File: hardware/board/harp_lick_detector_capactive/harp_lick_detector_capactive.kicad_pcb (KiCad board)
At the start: 4 copper layers, 80 x 50 mm, 132 parts, among them J1 Conn_Coaxial, J2 Conn_01x03_Male, J3 Conn_Triaxial, J4 AudioJack3, J5 USB_C_Receptacle_USB2.0, J6 Barrel_Jack_Switch, J7 Conn_Coaxial, SW1 SW_Push, U10 CD74AC04, U11 LM27762, U12 LT3030, U13 ADS7049, U2 TPD2EUSB30, U3 ADUM4160, U4 RP2040, U5 W25Q128JVS, U6 LTC6263, U7 LTC6268xS8-10, U8 REF3433QDBVRQ1, U9 AD9833xRM, X1 ECS-TXO-2016

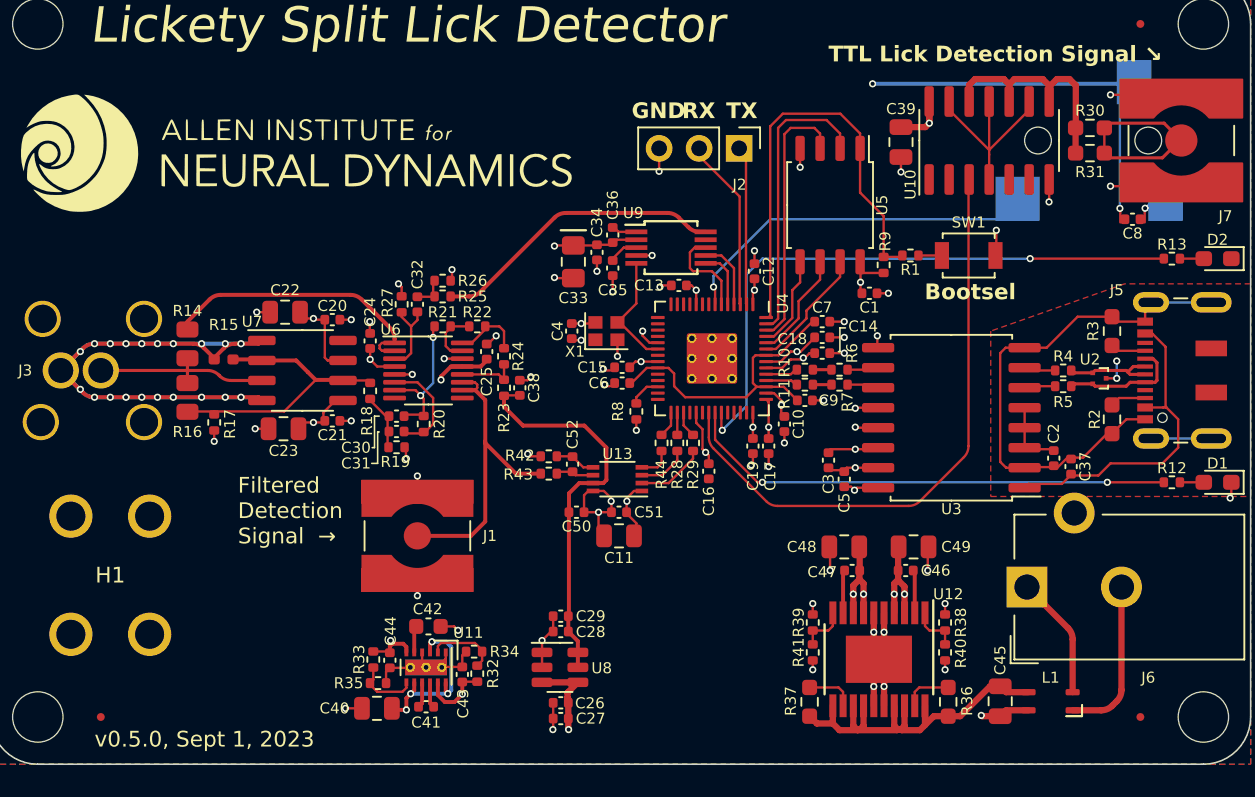
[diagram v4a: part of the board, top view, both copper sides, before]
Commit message: add tvs diodes; remove run pullup; finish trace guard
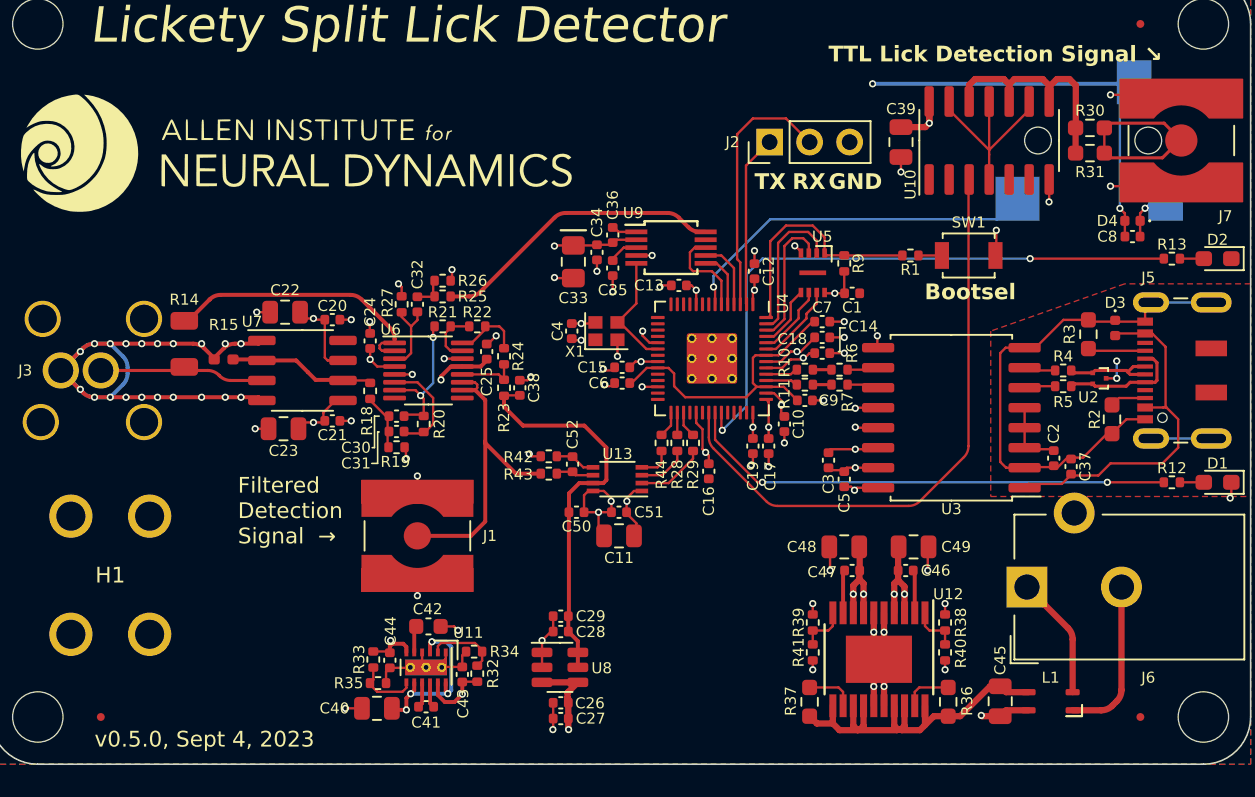
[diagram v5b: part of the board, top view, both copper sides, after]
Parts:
- removed R16: 100K, Resistor_SMD:R_0805_2012Metric
- removed R17: 100K, Resistor_SMD:R_0402_1005Metric
- removed R8: 10K, Resistor_SMD:R_0402_1005Metric
- added D3: D_TVS, Diode_SMD:D_0402_1005Metric, F.Cu at (176.3, 90.3)
- added D4: D_TVS, Diode_SMD:D_0402_1005Metric, F.Cu at (177.4, 83.5)
- R14: footprint Resistor_SMD:R_0805_2012Metric -> Resistor_SMD:R_1206_3216Metric
- R23, R24: value 1K -> 10K
- R27: value 100K -> 10K
- U5: value W25Q128JVS -> W25Q16JVUXIQ; footprint Package_SO:SOIC-8_5.23x5.23mm_P1.27mm -> kicad_component_library:Winbond-8USON-2x3mm
- moved U5 4.44 mm to (157.1, 86.8)
- moved R9 2.50 mm to (159.1, 86.2)
- moved J2 1.98 mm to (154.4, 78.5), turned to 90 degrees
- moved R3 1.51 mm to (174.6, 90.7)
- moved C1 1.10 mm to (159.6, 88.1)
- moved C8 1.10 mm to (177.4, 84.5)
- moved R14 0.20 mm to (117.2, 91.3)
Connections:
- U4 pad 26: Net-(U4-RUN) -> +3V3
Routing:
- net /Lick Detection Analog Front End/triax_inner_shield: track 54.3 -> 39.7 mm
- net /Harp Core RP2040 + Isolated USB/QSPI_CS: track 28.5 -> 15.1 mm
- net Net-(U7--): track 18.3 -> 9.28 mm
- net /Harp Core RP2040 + Isolated USB/QSPI_D1: track 18.4 -> 9.47 mm
- net /Harp Core RP2040 + Isolated USB/QSPI_D2: track 16.7 -> 8.58 mm
- net /Harp Core RP2040 + Isolated USB/UART0_RXD: track 11.0 -> 16.5 mm
- net /Harp Core RP2040 + Isolated USB/QSPI_D3: track 7.85 -> 5.28 mm
- net GND: track 94.9 -> 92.4 mm, vias 61 -> 58
- net /Harp Core RP2040 + Isolated USB/QSPI_CLK: track 6.86 -> 4.62 mm
- net Net-(U4-RUN): track 2.03 -> 0.00 mm
- net VBUS: track 20.5 -> 22.5 mm
- net /Harp Core RP2040 + Isolated USB/QSPI_D0: track 5.92 -> 3.99 mm
- net /Lick Detection Analog Front End/triax_core: track 12.0 -> 10.4 mm
- net Net-(J5-CC2): track 2.24 -> 3.66 mm
- net /Harp Core RP2040 + Isolated USB/UART0_TXD: track 10.1 -> 10.9 mm
- added copper zone on In1.Cu, net /Lick Detection Analog Front End/triax_inner_shield
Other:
- board text added: "Sonya Vasquez"
- board text added: "Sub-millisecond, ephys-compatible rodent lick detection system."
- board text added: "v0.5.0, Sept 4, 2023"
- board text removed: "Rodent lick detection sensing made lickety-split."
- board text removed: "Vasquez"
- board text removed: "v0.5.0, Sept 1, 2023"

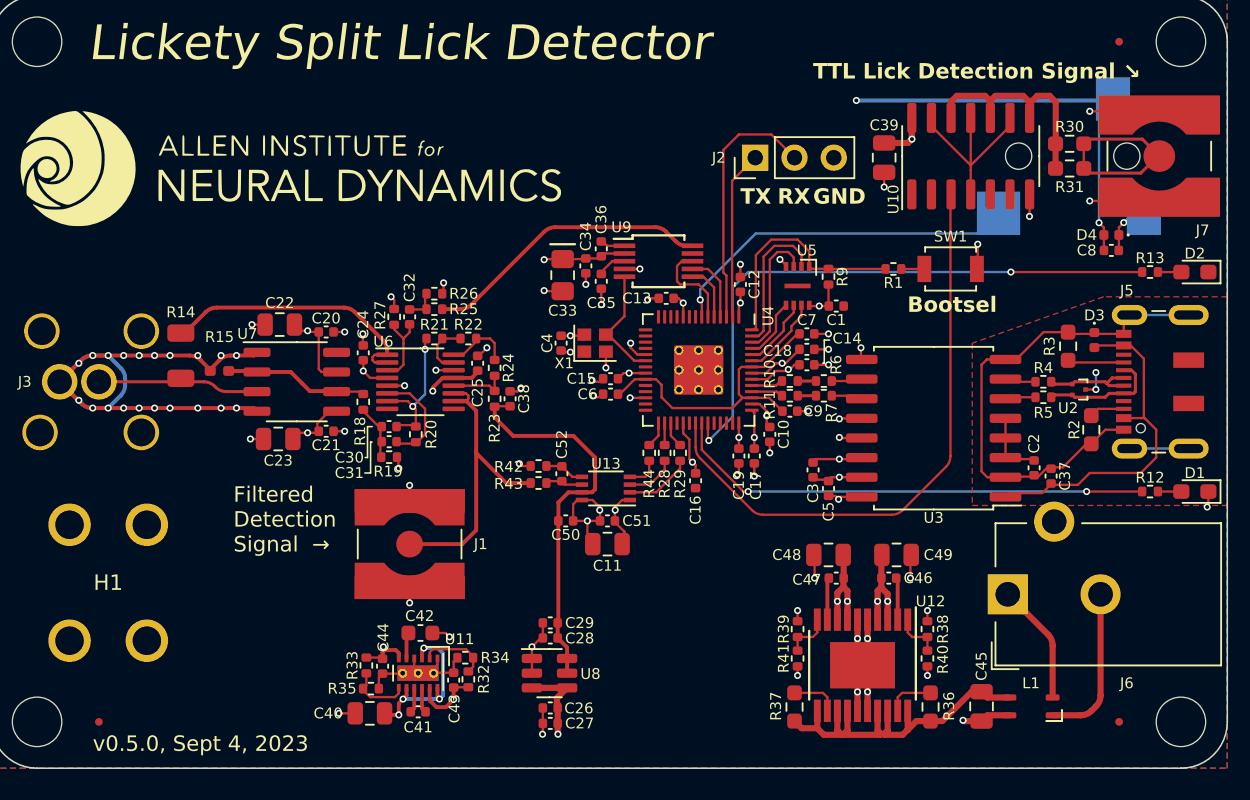
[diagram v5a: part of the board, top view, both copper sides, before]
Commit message: update ads7049 pinout
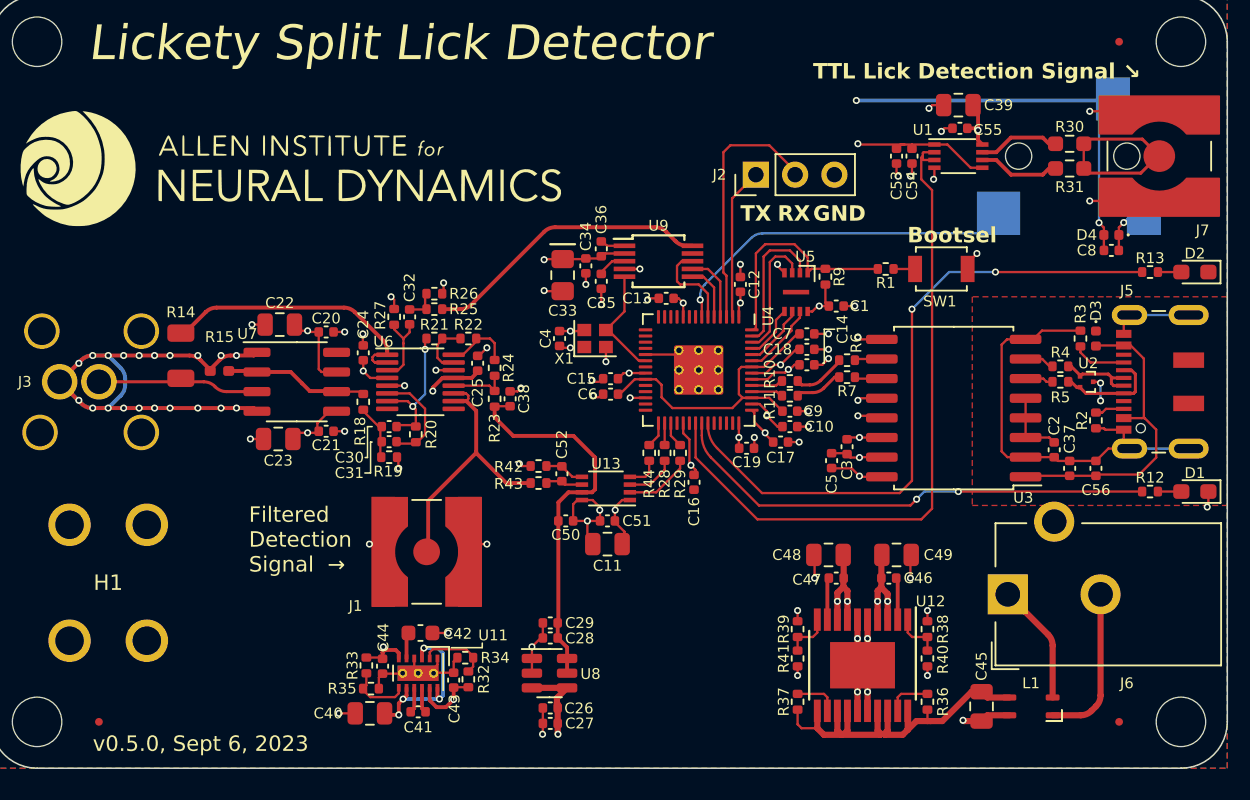
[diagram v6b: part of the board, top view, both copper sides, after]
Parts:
- removed U10: CD74AC04, Package_SO:SOIC-14_3.9x8.7mm_P1.27mm
- added C53: 1uF, Capacitor_SMD:C_0402_1005Metric, F.Cu at (163.5, 78.4)
- added C54: 100nF, Capacitor_SMD:C_0402_1005Metric, F.Cu at (164.5, 78.4)
- added C55: 100nF, Capacitor_SMD:C_0402_1005Metric, F.Cu at (167.6, 76.6)
- added C56: 1uF, Capacitor_SMD:C_0402_1005Metric, F.Cu at (176.4, 98.6)
- added U1: 74LVCH2T45DC, Package_SO:VSSOP-8_2.3x2mm_P0.5mm, F.Cu at (167.5, 78.4)
- R2, R3, R36, R37: footprint Resistor_SMD:R_0603_1608Metric_Pad0.98x0.95mm_HandSolder -> Resistor_SMD:R_0402_1005Metric
- moved C39 5.88 mm to (167.5, 75.1), turned to 180 degrees
- moved C3 2.66 mm to (160.3, 97.2)
- moved R6 2.02 mm to (160.3, 91.6)
- moved C17 1.92 mm to (156.0, 96.9), turned to 180 degrees
- moved R7 1.92 mm to (160.3, 92.7)
- moved U3 1.84 mm to (167.2, 94.7)
- moved C5 1.81 mm to (159.3, 98.1)
- moved C2 1.75 mm to (173.7, 97.4)
- moved R4 1.49 mm to (174.1, 92.0)
- moved R5 1.49 mm to (174.1, 93.0)
- moved C10 1.39 mm to (156.6, 95.9), turned to 0 degrees
- moved C37 1.30 mm to (174.7, 98.6)
- moved J1 1.21 mm to (133.1, 104.0), turned to 90 degrees
- moved J2 1.10 mm to (154.4, 79.6)
- moved R3 0.94 mm to (175.4, 90.2)
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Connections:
- R30 pad 1: Net-(R30-Pad1) -> Net-(U1-1B)
- R31 pad 1: Net-(R30-Pad1) -> Net-(U1-2B)
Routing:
- net Net-(R30-Pad1): track 17.2 -> 0.00 mm
- net Net-(U10-Pad11): track 13.2 -> 0.00 mm
- net +3V3: track 79.6 -> 90.6 mm, vias 23 -> 24
- net GND: track 92.4 -> 98.8 mm, vias 58 -> 61
- net /Harp Core RP2040 + Isolated USB/TTL_OUT: track 38.7 -> 44.5 mm
- net Net-(U1-1B): track 0.00 -> 4.87 mm
- net Net-(U1-2B): track 0.00 -> 4.87 mm
- net Net-(U4-GPIO25): track 38.6 -> 42.9 mm
- net GND1: track 38.5 -> 35.6 mm
- net /Harp Core RP2040 + Isolated USB/DD+: track 1.00 -> 3.46 mm
- net /Harp Core RP2040 + Isolated USB/DD-: track 1.00 -> 3.13 mm
- net Net-(J1-In): track 20.8 -> 18.7 mm
- net VBUS: track 22.5 -> 20.5 mm
- net IN1: track 24.6 -> 26.0 mm
- net +5V: track 28.7 -> 27.6 mm
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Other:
- board text added: "Vasquez"
- board text added: "v0.5.0, Sept 6, 2023"
- board text removed: "Sonya Vasquez"
- board text removed: "v0.5.0, Sept 4, 2023"

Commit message: draft v0.6.0 board
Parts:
- removed C29: 1uF, Capacitor_SMD:C_0402_1005Metric
- removed J1: Conn_Coaxial, Connector_Coaxial:SMA_Amphenol_132134-10_Vertical
- removed U9: AD9833xRM, Package_SO:MSOP-10_3x3mm_P0.5mm
- added C57: 1nF, Capacitor_SMD:C_0402_1005Metric, F.Cu at (136.8, 85.1)
- added C58: 1nF, Capacitor_SMD:C_0402_1005Metric, F.Cu at (133.8, 85.1)
- added C59: 100nF, Capacitor_SMD:C_0402_1005Metric, F.Cu at (138.7, 110.8)
- added R16: 4K7, Resistor_SMD:R_0402_1005Metric, F.Cu at (141.3, 85.6)
- added R17: 4K7, Resistor_SMD:R_0402_1005Metric, F.Cu at (138.3, 85.6)
- added R45: 4K7, Resistor_SMD:R_0402_1005Metric, F.Cu at (135.3, 85.6)
- added R46: 124, Resistor_SMD:R_0402_1005Metric, F.Cu at (129.1, 92.3)
- added R47: 127, Resistor_SMD:R_0402_1005Metric, F.Cu at (139.0, 92.1)
- added R48: 9K76, Resistor_SMD:R_0402_1005Metric, F.Cu at (136.0, 90.2)
- added R49: 1K02, Resistor_SMD:R_0402_1005Metric, F.Cu at (136.0, 89.2)
- added R52: 1K02, Resistor_SMD:R_0402_1005Metric, F.Cu at (137.7, 95.1)
- added R8: 4K7, Resistor_SMD:R_0402_1005Metric, F.Cu at (144.3, 85.6)
- added TP1: TestPoint, kicad_component_library:TestPoint_Keystone_5027_Miniature, F.Cu at (140.1, 100.7)
- C30, C31: value 160pF -> 150pF
- C32, C36: value 10nF -> 1nF
- C33: value 10uF -> 160pF; footprint Capacitor_SMD:C_0805_2012Metric_Pad1.18x1.45mm_HandSolder -> Capacitor_SMD:C_0402_1005Metric
- C34: value 100nF -> 160pF
- C35: value 100nF -> 1nF
- R12, R13: value 330 -> 680
- R18: value 49K9 -> 105K
- R20: value 100K -> 102K
- R21: value 68 -> 102K
- R22: value 10K -> 102K
- R23: value 10K -> 105K
- R24: value 10K -> 1K05
- R25: value 10K -> 4K7
- R26: value 330 -> 102K
- R27: value 10K -> 9K53
- R42, R43: value 16 -> 68
- SW1: value SW_Push -> ~; footprint Button_Switch_SMD:SW_SPST_B3U-1000P -> kicad_component_library:SW_Push_1P1T-SH_NO_Vertical_Wuerth_WS-TASV
- U8: value REF3433QDBVRQ1 -> REF2033; footprint Package_TO_SOT_SMD:SOT-23-6 -> Package_TO_SOT_SMD:SOT-23-5
- moved R21 7.07 mm to (138.7, 95.1), turned to -90 degrees
- moved C34 6.45 mm to (138.5, 89.7), turned to -90 degrees
- moved R23 6.09 mm to (136.0, 88.2), turned to 0 degrees
- moved R26 5.81 mm to (138.0, 91.1), turned to 180 degrees
- moved C33 5.69 mm to (137.5, 89.7)
- moved R22 5.61 mm to (136.1, 95.8), turned to 180 degrees
- moved R27 5.06 mm to (130.2, 93.8)
- moved C36 4.65 mm to (139.8, 85.1), turned to 90 degrees
- moved C4 4.03 mm to (145.2, 88.2), turned to 0 degrees
- moved R42 3.78 mm to (144.1, 98.1)
- moved R24 3.12 mm to (139.5, 89.7), turned to 90 degrees
- moved C28 3.06 mm to (143.9, 110.8), turned to 90 degrees
- moved G2 2.77 mm to (126.8, 78.0)
- moved C25 2.56 mm to (138.6, 93.1), turned to 0 degrees
- moved R25 2.30 mm to (131.7, 87.0), turned to 90 degrees
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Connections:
- net /100KHz Sine Wave/xtal_in renamed Net-(U4-XIN)
- C33 pad 1: +3V3 -> Net-(C33-Pad1)
- C33 pad 2: GND -> Net-(C33-Pad2)
- C34 pad 1: GND -> Net-(C33-Pad1)
- C34 pad 2: +3V3 -> Net-(U6D--)
- C35 pad 1: GND -> Net-(C35-Pad1)
- C35 pad 2: Net-(U9-CAP/2.5V) -> GND
- C36 pad 2: +3V3 -> GND
- C38 pad 2: VREF_3V3 -> VREF_1V65
- R21 pad 1: Net-(C30-Pad2) -> Net-(U6C-+)
- R21 pad 2: Net-(U6D--) -> VREF_1V65
- R22 pad 1: Net-(U6D--) -> Net-(R22-Pad1)
- R22 pad 2: Net-(R22-Pad2) -> Net-(U6C--)
- R23 pad 1: Net-(U6C-+) -> Net-(C30-Pad2)
- R23 pad 2: VREF_3V3 -> Net-(C33-Pad1)
- R24 pad 1: Net-(R22-Pad2) -> GND
- R24 pad 2: Net-(U6C-+) -> Net-(C33-Pad1)
- R25 pad 1: Net-(C32-Pad1) -> Net-(U6A-+)
- R25 pad 2: Net-(U9-VOUT) -> GND
- R26 pad 1: Net-(C32-Pad1) -> Net-(U6D--)
- R26 pad 2: GND -> Net-(C33-Pad2)
- R27 pad 1: GND -> Net-(U6B-+)
- R27 pad 2: Net-(U6A-+) -> Net-(C30-Pad2)
- R42 pad 1: Net-(U13-AINM) -> GND
- R42 pad 2: GND -> Net-(U13-AINM)
- R43 pad 1: Net-(J1-In) -> Net-(U13-AINP)
- R43 pad 2: Net-(U13-AINP) -> Net-(R22-Pad1)
- SW1 pad 1: GND -> unconnected-(SW1-Pad1)
- U4 pad 24: /Harp Core RP2040 + Isolated USB/SWCLK -> unconnected-(U4-SWCLK-Pad24)
- U4 pad 25: /Harp Core RP2040 + Isolated USB/SWDIO -> unconnected-(U4-SWD-Pad25)
- U4 pad 4: /100KHz Sine Wave/SCK -> /100KHz Sine Wave/100KHZ_SQ_WAVE_IN
- U4 pad 5: /100KHz Sine Wave/PICO -> unconnected-(U4-GPIO3-Pad5)
- U4 pad 6: /100KHz Sine Wave/CS -> unconnected-(U4-GPIO4-Pad6)
- U6 pad 10: Net-(J1-In) -> Net-(R22-Pad1)
- U6 pad 11: Net-(J1-In) -> Net-(U6C--)
- U6 pad 14: GND -> Net-(U6D-+)
- U6 pad 16: Net-(R22-Pad2) -> Net-(C33-Pad2)
- U6 pad 5: GND -> Net-(U6B-+)
- U8 pad 1: GND -> VREF_1V65
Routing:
- net Net-(J1-In): track 18.7 -> 0.00 mm
- net Net-(U9-VOUT): track 18.6 -> 0.00 mm
- net VREF_1V65: track 0.00 -> 17.2 mm, vias 0 -> 2
- net Net-(R22-Pad1): track 0.00 -> 12.2 mm
- net VREF_3V3: track 25.1 -> 13.4 mm
- net /100KHz Sine Wave/100KHZ_SQ_WAVE_IN: track 0.00 -> 9.28 mm
- net GND: track 98.8 -> 107.3 mm, vias 61 -> 76
- net /100KHz Sine Wave/CS: track 5.96 -> 0.00 mm
- net Net-(U6D-+): track 0.00 -> 5.66 mm
- net Net-(U4-XIN): track 7.33 -> 1.74 mm
- net Net-(U6C-+): track 3.77 -> 9.35 mm
- net +3V3: track 90.6 -> 85.4 mm
- net Net-(U6C--): track 0.00 -> 5.18 mm
- net /100KHz Sine Wave/SCK: track 4.43 -> 0.00 mm
- net Net-(C33-Pad2): track 0.00 -> 4.42 mm
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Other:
- board text added: "Filtered ↗ Detection Signal"
- board text added: "Setup Notes: • The animal must share a ground with this board through the ground lug. • USB and 3.5mm (Harp) connections are not needed if solely using the TTL output."
- board text added: "Sonya Vasquez"
- board text added: "v0.6.0, Oct 13, 2023"
- board text removed: "Filtered Detection Signal →"
- board text removed: "Setup Notes: • The ground lug must be connected to the chassis ground of the rig. • USB and 3.5mm (Harp) connections are not needed if solely using the TTL output."
- board text removed: "Vasquez"
- board text removed: "v0.5.0, Sept 6, 2023"

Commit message: make r0.6 board snapshot
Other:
- board text added: "v0.6.0, Oct 16, 2023"
- board text removed: "v0.6.0, Oct 13, 2023"
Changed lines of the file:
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@@
       (disableapertmacros false)
       (usegerberextensions true)
-      (usegerberattributes true)
+      (usegerberattributes false)
       (usegerberadvancedattributes true)
       (creategerberjobfile true)
@@
       (drillshape 0)
       (scaleselection 1)
-      (outputdirectory "exports/lickety_split_r0.5/gerbers/")
+      (outputdirectory "exports/lickety_split_r0.6/gerbers/")
     )
   )
@@
     (fp_line (start -1.27 3.4798) (end 1.27 3.4798)
       (stroke (width 0.12) (type solid)) (layer "F.Fab"))
-    (pad "1" thru_hole circle (at 0 0 90) (size 2.3 2.3) (drill 1.5875) (layers "*.Cu" "*.Mask")
+    (pad "1" thru_hole circle (at 0 0 90) (size 2.2 2.2) (drill 1.5875) (layers "*.Cu" "*.Mask")
       (net 25 "/Lick Detection Analog Front End/triax_core") (pinfunction "In") (pintype "passive"))
-    (pad "2" thru_hole circle (at 0 -2.54 90) (size 2.3 2.3) (drill 1.5875) (layers "*.Cu" "*.Mask")
+    (pad "2" thru_hole circle (at 0 -2.54 90) (size 2.2 2.2) (drill 1.5875) (layers "*.Cu" "*.Mask")
       (net 30 "/Lick Detection Analog Front End/triax_inner_shield") (pinfunction "Guard") (pintype "passive"))
     (pad "3" thru_hole circle (at -3.2766 -3.81 90) (size 2.3 2.3) (drill 1.8) (layers "*.Cu" "*.Mask")
@@
           (width 0.1) (fill yes))
       ))
-    (model "${KICAD6_3DMODEL_DIR}/Connector_Coaxial.3dshapes/SMA_Amphenol_132134-10_Vertical.wrl"
-      (offset (xyz 0 0 0))
+    (model "/home/poofjunior/projects/kicad_libraries/kicad_component_library/kicad_component_library.3dshapes/CONSMA002-SMD-G-T.step"
+      (offset (xyz -4.1 -0 0))
       (scale (xyz 1 1 1))
-      (rotate (xyz 0 0 0))
+      (rotate (xyz -90 0 90))
     )
   )
@@
     (effects (font (size 2.25 2.25) (thickness 0.4) italic) (justify left bottom))
   )
-  (gr_text "v0.6.0, Oct 13, 2023" (at 111.5 117) (layer "F.SilkS")
+  (gr_text "v0.6.0, Oct 16, 2023" (at 111.5 117) (layer "F.SilkS")
     (effects (font (size 1 1) (thickness 0.15)) (justify left bottom))
   )
